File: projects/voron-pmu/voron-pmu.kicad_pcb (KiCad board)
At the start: 2 copper layers, 107 x 72 mm, 17 parts, among them J1 Critical loads, J2 Non-critical loads, J3 Critical supply, J4 Non-critical supply, J5 Pwr-loss-1, J6 Pwr-loss-2, K1 G2RL-2, K2 G2RL-2, K3 G2RL-2, K4 FINDER-40.52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

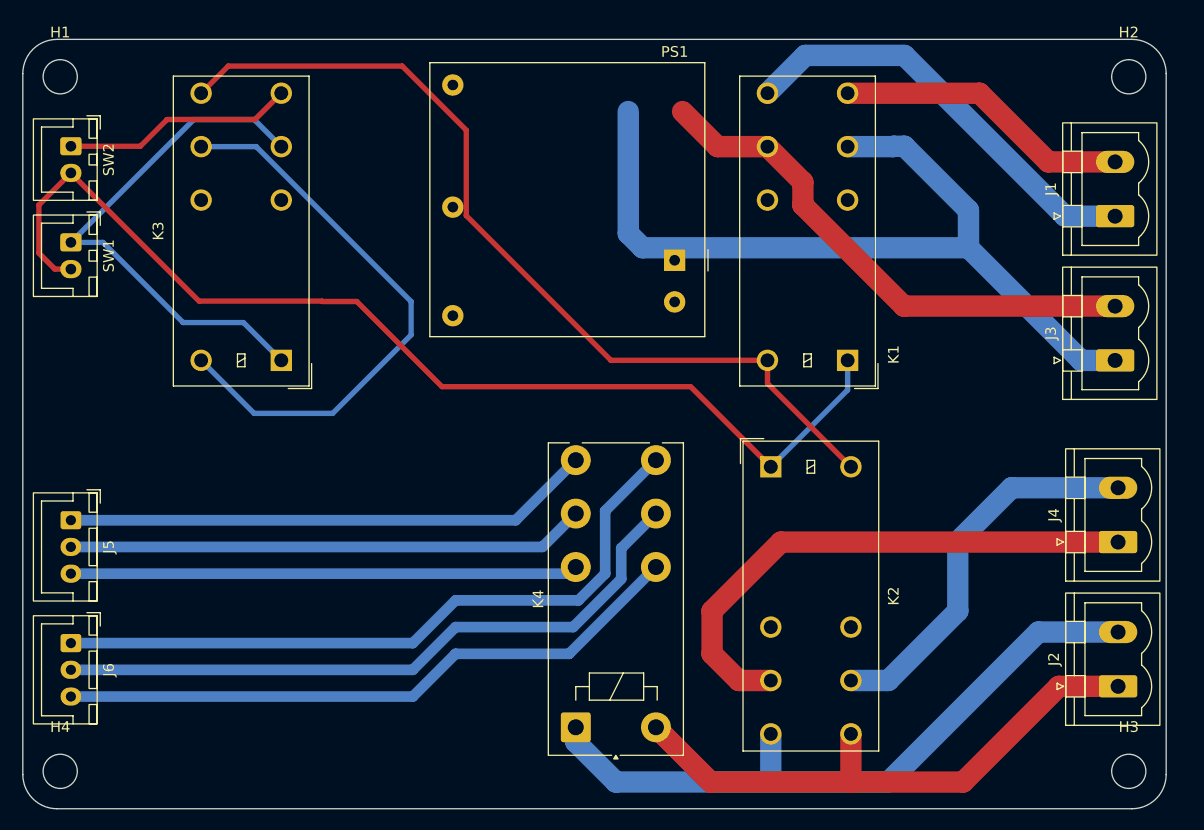
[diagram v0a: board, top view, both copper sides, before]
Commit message: Adding pwr-good and stby indications.
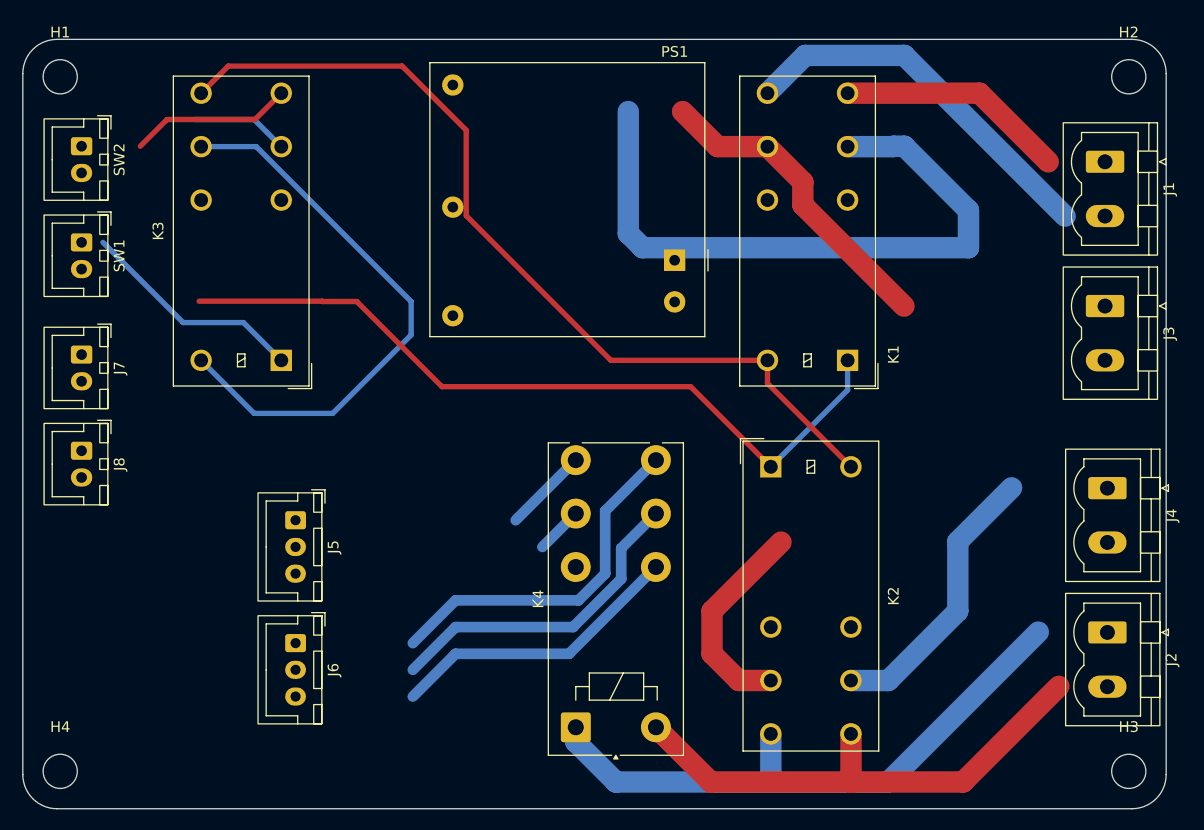
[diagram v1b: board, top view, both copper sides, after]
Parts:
- added J7: pwr-on, Connector_JST:JST_XH_B2B-XH-A_1x02_P2.50mm_Vertical, F.Cu at (102.0, 76.0)
- added J8: stby, Connector_JST:JST_XH_B2B-XH-A_1x02_P2.50mm_Vertical, F.Cu at (102.0, 85.0)
- moved J5 21.0 mm to (122.0, 91.5)
- moved J6 21.0 mm to (122.0, 103.0)
- moved J1 5.18 mm to (197.8, 58.0), turned to -90 degrees
- moved J3 5.18 mm to (197.8, 71.5), turned to -90 degrees
- moved J2 5.14 mm to (198.0, 102.0), turned to -90 degrees
- moved J4 5.14 mm to (198.0, 88.5), turned to -90 degrees
- moved SW1 1.00 mm to (102.0, 65.5)
- moved SW2 1.00 mm to (102.0, 56.5)
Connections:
- K3 pad 22: unconnected-(K3-Pad22) -> Net-(J8-Pin_2)
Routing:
- net Net-(J5-Pin_3): track 47.5 -> 0.88 mm
- net Net-(J5-Pin_2): track 48.5 -> 4.42 mm
- net Net-(J5-Pin_1): track 49.6 -> 7.95 mm
- net Net-(J6-Pin_3): track 59.8 -> 27.8 mm
- net Net-(J6-Pin_2): track 62.5 -> 30.5 mm
- net Net-(J6-Pin_1): track 65.3 -> 33.3 mm
- net Net-(J4-Pin_1): track 51.2 -> 19.7 mm
- net GND: track 102.2 -> 72.9 mm
- net Net-(J3-Pin_2): track 49.3 -> 29.5 mm
- net Net-(K3-Pad11): track 49.8 -> 30.5 mm
- net Net-(J3-Pin_1): track 79.2 -> 61.1 mm
- net Net-(J4-Pin_2): track 36.3 -> 26.3 mm
- net Net-(J2-Pin_2): track 64.2 -> 56.7 mm
- net Net-(SW2-A): track 21.7 -> 15.2 mm
- net Net-(J1-Pin_2): track 27.7 -> 21.4 mm
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
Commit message: Routing a new revision.
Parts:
- PS1: footprint Converter_ACDC:Converter_ACDC_RECOM_RAC05-xxSK_THT -> Converter_ACDC:Converter_ACDC_RECOM_RAC04-xxSGx_THT
- moved J5 21.3 mm to (102.3, 99.5)
- moved J6 15.9 mm to (109.2, 112.5), turned to 0 degrees
- moved PS1 7.21 mm to (160.2, 60.5), turned to -90 degrees
- moved K1 3.26 mm to (175.5, 79.2)
- moved K3 2.48 mm to (121.0, 79.0)
- moved J1 1.75 mm to (196.0, 58.0)
- moved J2 1.75 mm to (196.2, 102.0)
- moved J3 1.75 mm to (196.0, 71.5)
- moved J4 1.75 mm to (196.2, 88.5)
- moved K2 1.68 mm to (168.0, 85.8)
- moved K4 1.00 mm to (148.2, 109.9)
- moved J7 0.25 mm to (102.2, 76.0)
- moved J8 0.25 mm to (102.2, 85.0)
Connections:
- net Net-(J3-Pin_1) renamed /neutral-in
- net Net-(J3-Pin_2) renamed /line-in
- net Net-(J4-Pin_1) renamed /neutral-in-aux
- net Net-(J4-Pin_2) renamed /line-in-aux
- J1 pad 1: Net-(J1-Pin_1) -> /neutral-critical
- J1 pad 2: Net-(J1-Pin_2) -> /line-critical
- J2 pad 1: Net-(J2-Pin_1) -> /neutral-non-critical
- J2 pad 2: Net-(J2-Pin_2) -> /line-non-critical
- K1 pad 14: Net-(J1-Pin_2) -> /neutral-critical
- K1 pad 24: Net-(J1-Pin_1) -> /line-critical
- K2 pad 14: Net-(J2-Pin_2) -> /neutral-non-critical
- K2 pad 24: Net-(J2-Pin_1) -> /line-non-critical
- K3 pad 11: Net-(K3-Pad11) -> Net-(SW2-B)
- K3 pad 14: Net-(SW2-A) -> +24V
- K3 pad A1: Net-(K3-Pad11) -> GND
- K3 pad A2: +24V -> Net-(SW2-A)
- K4 pad A1: Net-(J2-Pin_2) -> /neutral-non-critical
- K4 pad A2: Net-(J2-Pin_1) -> /line-non-critical
- SW1 pad 1: Net-(K3-Pad11) -> +24V
- SW1 pad 2: GND -> Net-(SW2-A)
- SW2 pad 2: GND -> Net-(SW2-B)
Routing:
- net /neutral-non-critical: track 0.00 -> 60.4 mm
- net Net-(J2-Pin_2): track 56.7 -> 0.00 mm
- net /line-non-critical: track 0.00 -> 50.9 mm
- net Net-(J5-Pin_3): track 0.88 -> 50.0 mm
- net Net-(J2-Pin_1): track 48.0 -> 0.00 mm
- net Net-(J5-Pin_2): track 4.42 -> 51.0 mm
- net Net-(J5-Pin_1): track 7.95 -> 52.0 mm
- net Net-(J1-Pin_1): track 35.6 -> 0.00 mm
- net /line-critical: track 0.00 -> 34.8 mm
- net Net-(J6-Pin_1): track 33.3 -> 65.7 mm
- net Net-(K3-Pad11): track 30.5 -> 0.00 mm
- net Net-(J8-Pin_2): track 0.00 -> 30.1 mm
- net +24V-sw: track 83.3 -> 113.2 mm
- net Net-(J6-Pin_2): track 30.5 -> 58.5 mm
- net /line-in: track 29.5 -> 55.4 mm
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
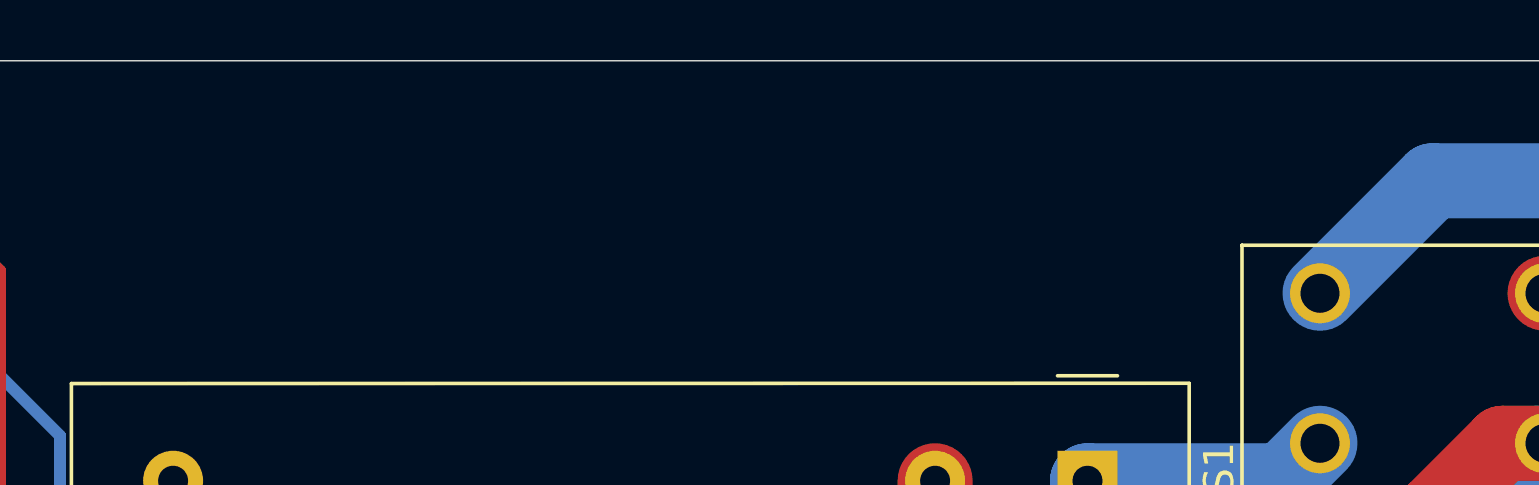
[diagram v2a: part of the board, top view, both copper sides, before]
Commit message: Adding labels.
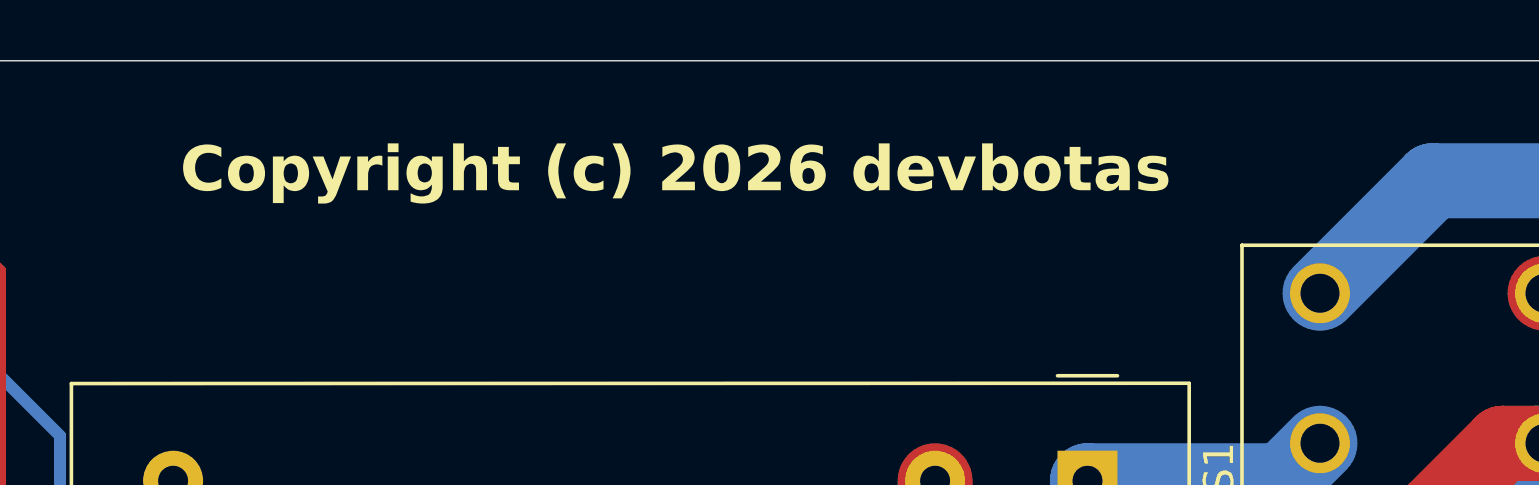
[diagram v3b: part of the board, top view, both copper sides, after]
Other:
- board text added: "Copyright (c) 2026 devbotas"
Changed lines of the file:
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@@
 		(layer "Edge.Cuts")
+	)
+	(gr_text "Copyright (c) 2026 devbotas"
+		(at 130 51 0)
+		(layer "F.SilkS")
+		(effects
+			(font
+				(size 1.5 1.5)
+				(thickness 0.3)
+				(bold yes)
+			)
+			(justify left bottom)
+		)
 	)
 	(segment

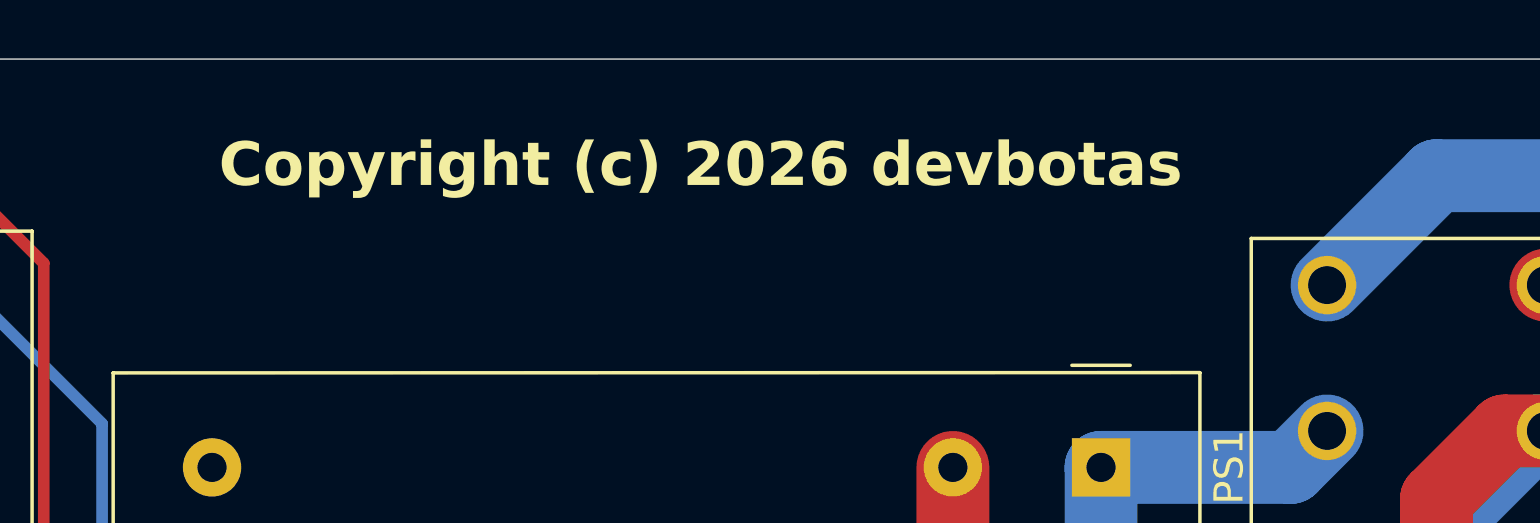
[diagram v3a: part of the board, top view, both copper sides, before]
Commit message: Adding mounting models and some other tweaks.
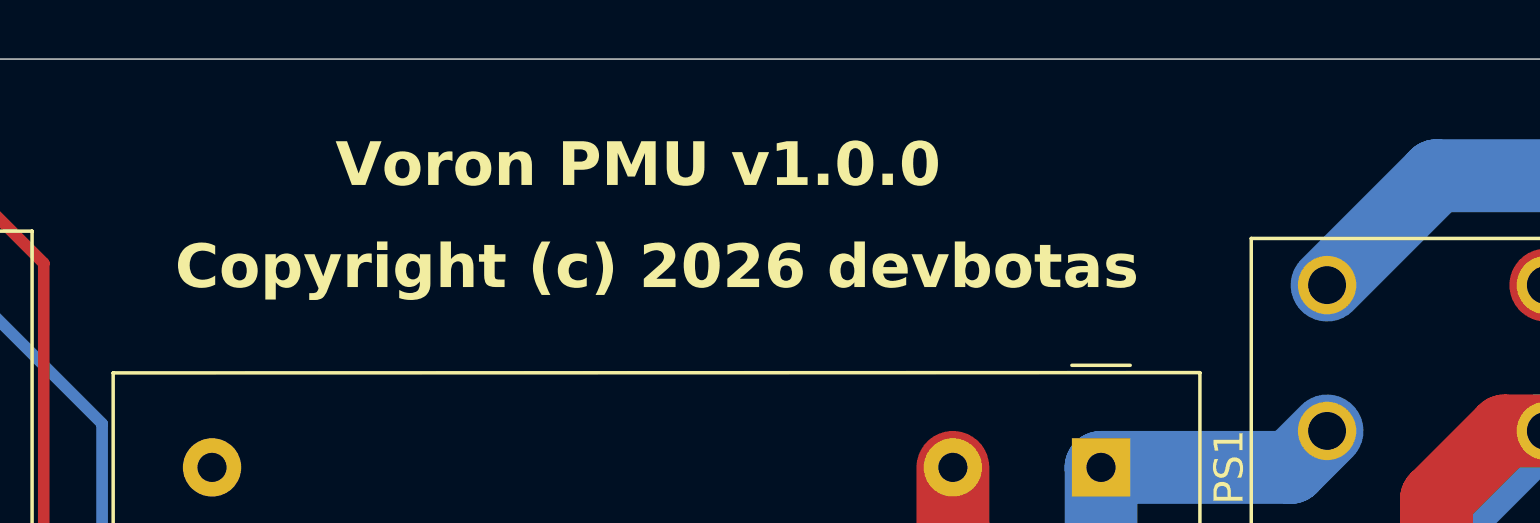
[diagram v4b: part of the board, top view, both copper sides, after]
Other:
- board text added: "Voron PMU v1.0.0"
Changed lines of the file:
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@@
 			(outputformat 1)
 			(mirror no)
-			(drillshape 1)
+			(drillshape 0)
 			(scaleselection 1)
-			(outputdirectory "")
+			(outputdirectory "ouput")
 		)
 	)
@@
 			)
 			(rotate
-				(xyz 0 0 0)
+				(xyz -0 -0 90)
 			)
 		)
@@
 			)
 			(rotate
-				(xyz 0 0 0)
+				(xyz -0 -0 90)
 			)
 		)
@@
 			)
 			(rotate
-				(xyz 0 0 0)
+				(xyz -0 -0 90)
 			)
 		)
@@
 	)
 	(gr_text "Copyright (c) 2026 devbotas"
-		(at 130 51 0)
+		(at 128.5 54.5 0)
+		(layer "F.SilkS")
+		(effects
+			(font
+				(size 1.5 1.5)
+				(thickness 0.3)
+				(bold yes)
+			)
+			(justify left bottom)
+		)
+	)
+	(gr_text "Voron PMU v1.0.0"
+		(at 134 51 0)
 		(layer "F.SilkS")
 		(effects
